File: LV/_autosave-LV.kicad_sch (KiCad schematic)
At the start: 21 parts

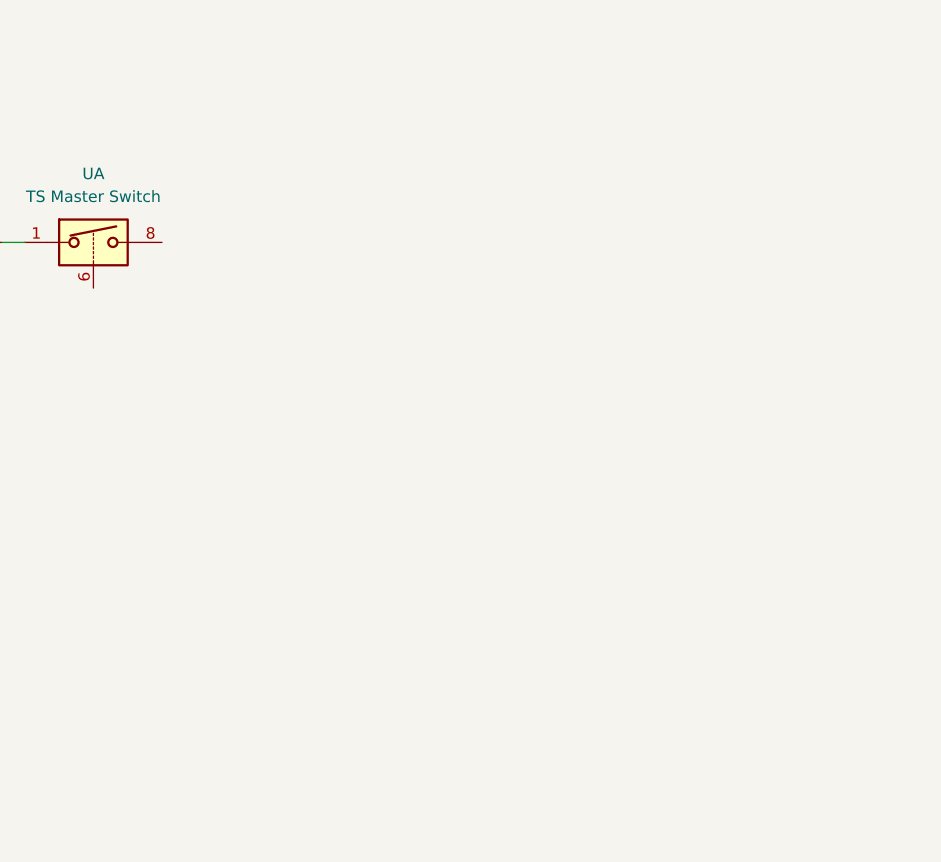
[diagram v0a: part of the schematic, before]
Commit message: Updated to KiCad 8.0 and continued work on shutdown circuit
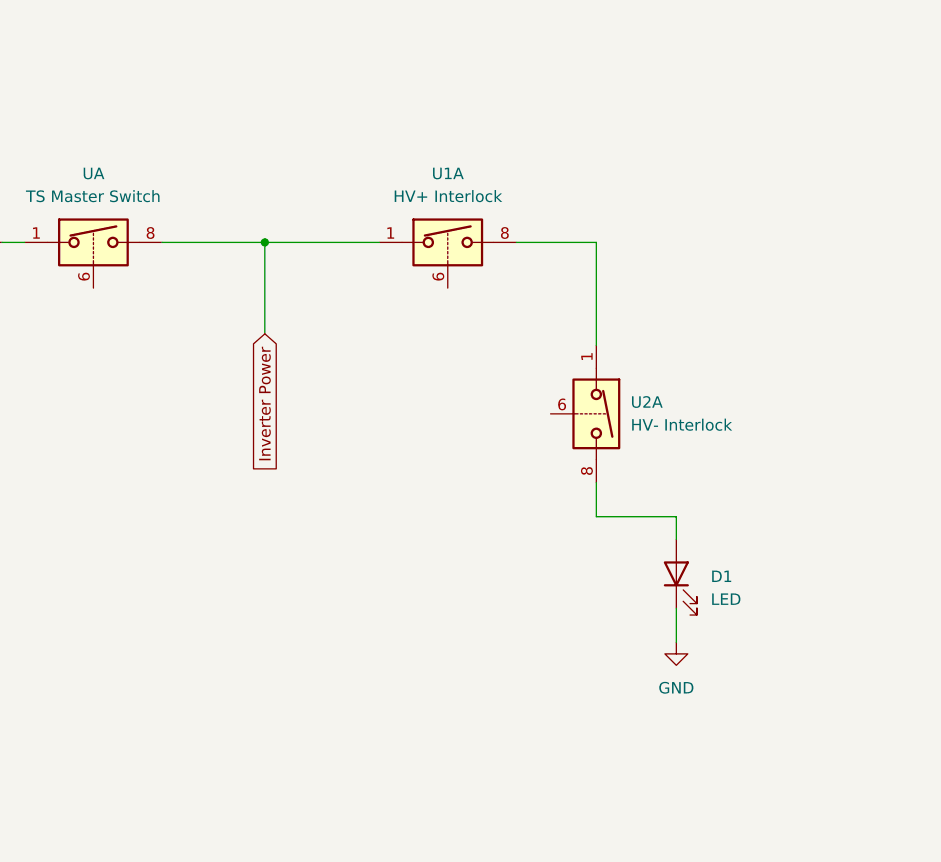
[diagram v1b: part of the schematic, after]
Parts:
- added D1: LED, symbol Device:LED
- added U1: HV+ Interlock, Package_DIP:DIP-8_W7.62mm, symbol Analog_Switch:ADG417BN
- added U2: HV- Interlock, Package_DIP:DIP-8_W7.62mm, symbol Analog_Switch:ADG417BN
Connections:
- net GND: now also D1.1 (K)
- net Inverter Power: now reaches U.8
- net Inverter Power: now also U1.1
- new net: U1.8, U2.1
- new net: D1.2 (A), U2.8
